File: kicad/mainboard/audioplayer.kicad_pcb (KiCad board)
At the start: 2 copper layers, 100 x 75 mm, 38 parts, among them J1 Panel, J2 Charge_USB, J3 SPK, J4 RFID, SW1 POWER, U1 PB-500, U2 ESP32-nodeMCU, U3 OLED, U4 GY-521, U5 VS1053/SD_breakout, U6 ULN2003, U7 HW-323

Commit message: board rev04
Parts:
- removed D1: 1N4007, Diode_THT:D_DO-41_SOD81_P10.16mm_Horizontal
- removed SW1: POWER, Connector_PinHeader_2.54mm:PinHeader_1x02_P2.54mm_Vertical
- added R4: ?, Resistor_THT:R_Axial_DIN0204_L3.6mm_D1.6mm_P7.62mm_Horizontal, F.Cu at (39.2, 90.7)
- added R5: ?, Resistor_THT:R_Axial_DIN0204_L3.6mm_D1.6mm_P7.62mm_Horizontal, F.Cu at (39.2, 88.5)
- added R7: 47k, Resistor_THT:R_Axial_DIN0204_L3.6mm_D1.6mm_P7.62mm_Horizontal, F.Cu at (42.3, 97.6)
- added TP4: R, Connector_PinHeader_2.54mm:PinHeader_1x01_P2.54mm_Vertical, F.Cu at (28.6, 89.6)
- J2: value Charge_USB -> Conn_02x04_Odd_Even; footprint Connector_PinHeader_2.54mm:PinHeader_1x02_P2.54mm_Vertical -> Connector_PinHeader_2.54mm:PinHeader_2x04_P2.54mm_Vertical
- moved J2 30.0 mm to (28.4, 60.9)
- moved R9 1.19 mm to (69.0, 112.1)
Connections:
- J1 pad 3: /LED4_OD -> /LED1_OD
- J1 pad 4: SW4 -> GND
- J1 pad 5: /LED3_OD -> /LED2_OD
- J1 pad 7: /LED2_OD -> /LED3_OD
- J1 pad 9: /LED1_OD -> /LED4_OD
- J2 pad 1: Net-(D1-Pad2) -> /USB+
- R2 pad 2: Net-(R2-Pad2) -> Net-(J2-Pad4)
- RN1 pad 5: SW4 -> GNDA
- U1 pad 1: Net-(D1-Pad1) -> /USB+
- U1 pad 3: Net-(R2-Pad2) -> Net-(J2-Pad4)
- U1 pad 4: Net-(SW1-Pad1) -> Net-(J2-Pad3)
- U2 pad 6: SW4 -> GNDA
- U6 pad 13: /LED4_OD -> /LED1_OD
- U6 pad 14: /LED3_OD -> /LED2_OD
- U6 pad 15: /LED2_OD -> /LED3_OD
- U6 pad 16: /LED1_OD -> /LED4_OD
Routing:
- net SW4: track 78.4 -> 0.00 mm
- net GNDA: track 113.0 -> 185.5 mm, vias 0 -> 4
- net Net-(J2-Pad3): track 0.00 -> 62.9 mm
- net /USB+: track 0.00 -> 53.6 mm
- net GND: track 322.5 -> 374.1 mm
- net Net-(J2-Pad4): track 0.00 -> 43.4 mm
- net Net-(J2-Pad5): track 0.00 -> 31.2 mm
- net Net-(J2-Pad8): track 0.00 -> 29.8 mm
- net Net-(SW1-Pad1): track 27.5 -> 0.00 mm
- net /AMP_ENABLE: track 84.4 -> 99.9 mm
- net Net-(R4-Pad2): track 0.00 -> 5.09 mm
- net Net-(D1-Pad2): track 5.08 -> 0.00 mm
- net /SCK: track 51.3 -> 55.6 mm
- net Net-(D1-Pad1): track 3.92 -> 0.00 mm
- net +5V: track 255.8 -> 259.4 mm
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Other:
- board text added: "MP3-DUCK rev 04"
- board text removed: "MP3-DUCK rev 03"

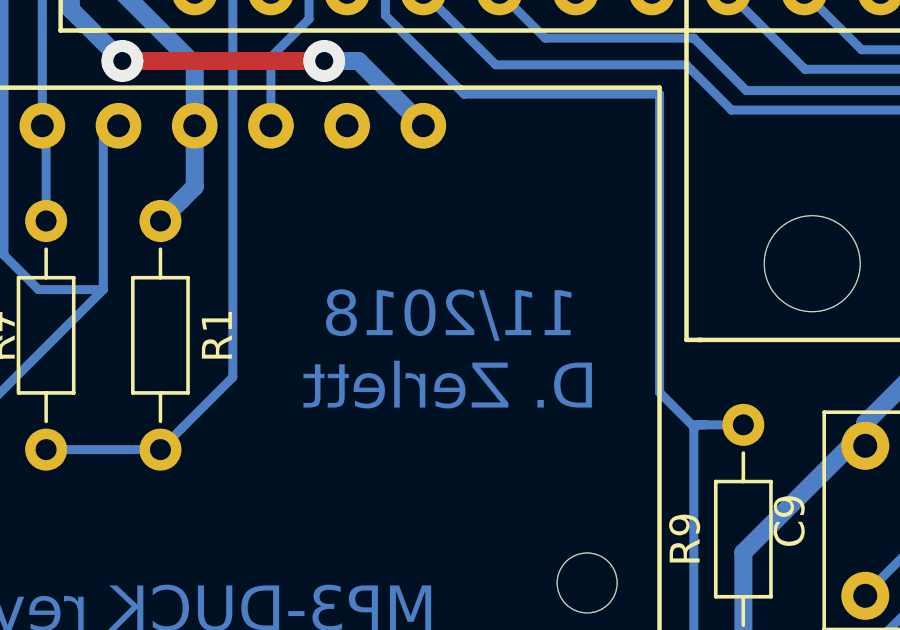
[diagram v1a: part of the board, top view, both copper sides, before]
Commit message: case changed et al
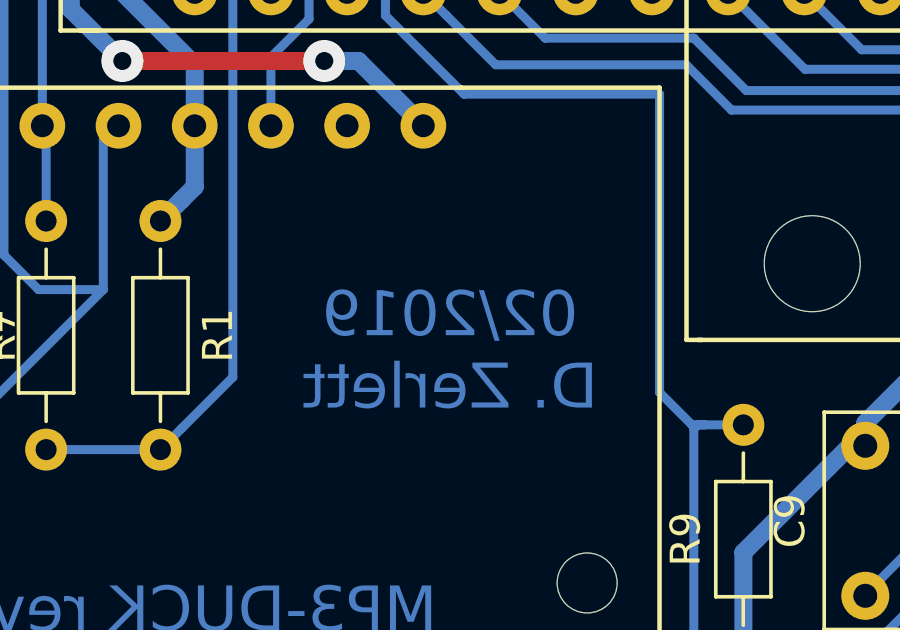
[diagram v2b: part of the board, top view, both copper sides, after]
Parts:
- R4: value ? -> 470
- R5: value ? -> 1k
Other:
- board text added: "02/2019 D. Zerlett"
- board text removed: "11/2018 D. Zerlett"
